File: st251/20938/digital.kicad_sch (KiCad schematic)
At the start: 25 parts, among them Y1 Crystal_Small, Y2 Crystal_Small

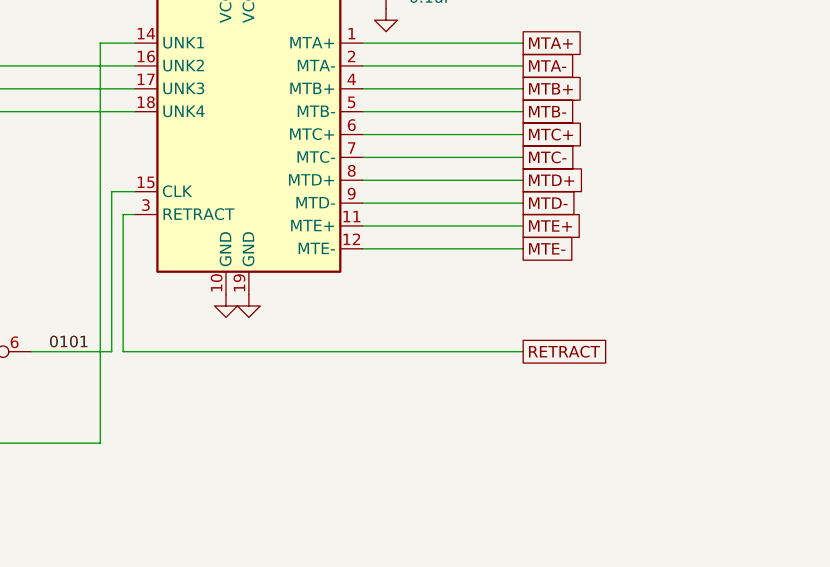
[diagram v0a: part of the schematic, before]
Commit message: Added description for RETURN ASIC
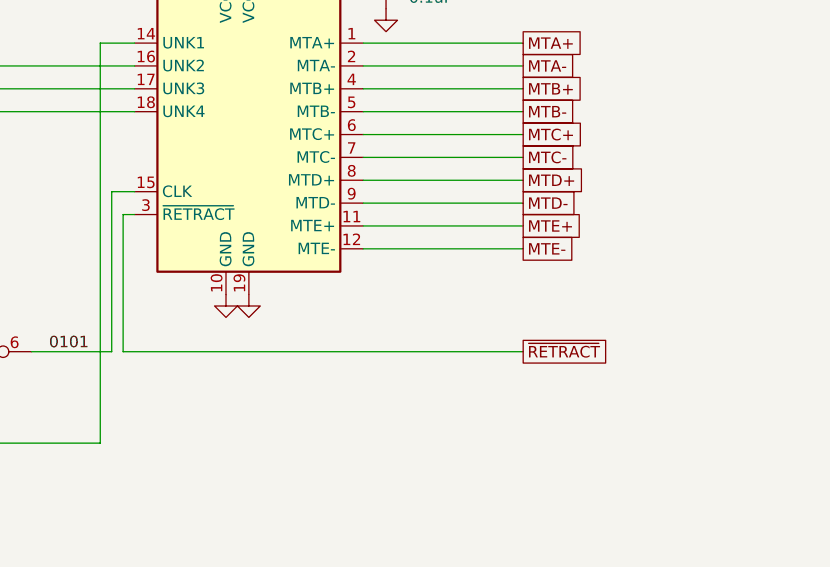
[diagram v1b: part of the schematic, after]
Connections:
- net RETRACT renamed ~{RETRACT}
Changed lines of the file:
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@@
     )
   )
-  (global_label "RETRACT" (shape passive) (at 355.6 139.7 0) (fields_autoplaced)
+  (global_label "~{RETRACT}" (shape passive) (at 355.6 139.7 0) (fields_autoplaced)
     (effects (font (size 1.27 1.27)) (justify left))
     (property "Intersheetrefs" "${INTERSHEET_REFS}" (at 365.4567 139.7 0)

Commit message: Add stepper sequencer documentation
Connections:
- net L_STEP?: now reaches 2B1.39 (UNK14), 3A1.31 (PA2)
- net L_TRK0_OUT: now reaches 2B1.5 (UNK15), 3A1.41 (PB0)
- net ~{HALFSTEP}: now reaches 6C1.16 (Q6), 7C1.16 (~{HALFSTEP})
- net DIRECTION: now reaches 6C1.15 (Q5), 7C1.17 (DIRECTION)
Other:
- note added: "<-"
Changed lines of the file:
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@@
     (stroke (width 0) (type default))
   )
-  (wire (pts (xy 287.02 93.98) (xy 287.02 110.49))
+  (wire (pts (xy 303.53 93.98) (xy 303.53 110.49))
     (stroke (width 0) (type default))
   )
@@
     (stroke (width 0) (type default))
   )
-  (wire (pts (xy 276.86 93.98) (xy 287.02 93.98))
+  (wire (pts (xy 276.86 93.98) (xy 303.53 93.98))
     (stroke (width 0) (type default))
   )
@@
     (stroke (width 0) (type default))
   )
-  (wire (pts (xy 287.02 110.49) (xy 312.42 110.49))
+  (wire (pts (xy 303.53 110.49) (xy 312.42 110.49))
     (stroke (width 0) (type default))
   )
@@
     (stroke (width 0) (type default))
   )
-  (wire (pts (xy 276.86 96.52) (xy 289.56 96.52))
+  (wire (pts (xy 276.86 96.52) (xy 300.99 96.52))
     (stroke (width 0) (type default))
   )
@@
     (stroke (width 0) (type default))
   )
-  (wire (pts (xy 289.56 96.52) (xy 289.56 107.95))
+  (wire (pts (xy 300.99 96.52) (xy 300.99 107.95))
     (stroke (width 0) (type default))
   )
@@
     (stroke (width 0) (type default))
   )
-  (wire (pts (xy 289.56 107.95) (xy 312.42 107.95))
+  (wire (pts (xy 300.99 107.95) (xy 312.42 107.95))
     (stroke (width 0) (type default))
   )
@@
     (effects (font (size 1.27 1.27)) (justify left bottom))
   )
+  (text "<-" (at 71.12 82.55 0)
+    (effects (font (size 1.27 1.27)) (justify left bottom))
+  )
   (text "ST-251 LSI FA CONTROL" (at 302.26 260.35 0)
     (effects (font (size 3.81 3.81)) (justify left bottom))
@@
     (effects (font (size 1.27 1.27)) (justify right bottom))
   )
+  (label "L_TRK0_OUT" (at 74.93 82.55 0) (fields_autoplaced)
+    (effects (font (size 1.27 1.27)) (justify left bottom))
+  )
   (label "L_DIR" (at 73.66 74.93 0) (fields_autoplaced)
     (effects (font (size 1.27 1.27)) (justify left bottom))
@@
     (effects (font (size 1.27 1.27)) (justify left bottom))
   )
+  (label "~{HALFSTEP}" (at 288.29 96.52 0) (fields_autoplaced)
+    (effects (font (size 1.27 1.27)) (justify left bottom))
+  )
   (label "A2" (at 148.59 74.93 180) (fields_autoplaced)
     (effects (font (size 1.27 1.27)) (justify right bottom))
@@
     (effects (font (size 1.27 1.27)) (justify left bottom))
   )
+  (label "INDEX_SYNC" (at 267.97 120.65 0) (fields_autoplaced)
+    (effects (font (size 1.27 1.27)) (justify left bottom))
+  )
+  (label "L_STEP?" (at 73.66 77.47 0) (fields_autoplaced)
+    (effects (font (size 1.27 1.27)) (justify left bottom))
+  )
   (label "D0" (at 160.02 101.6 0) (fields_autoplaced)
     (effects (font (size 1.27 1.27)) (justify left bottom))
@@
     (effects (font (size 1.27 1.27)) (justify right bottom))
   )
+  (label "DIRECTION" (at 292.1 93.98 0) (fields_autoplaced)
+    (effects (font (size 1.27 1.27)) (justify left bottom))
+  )
   (label "PHI2" (at 246.38 149.86 0) (fields_autoplaced)

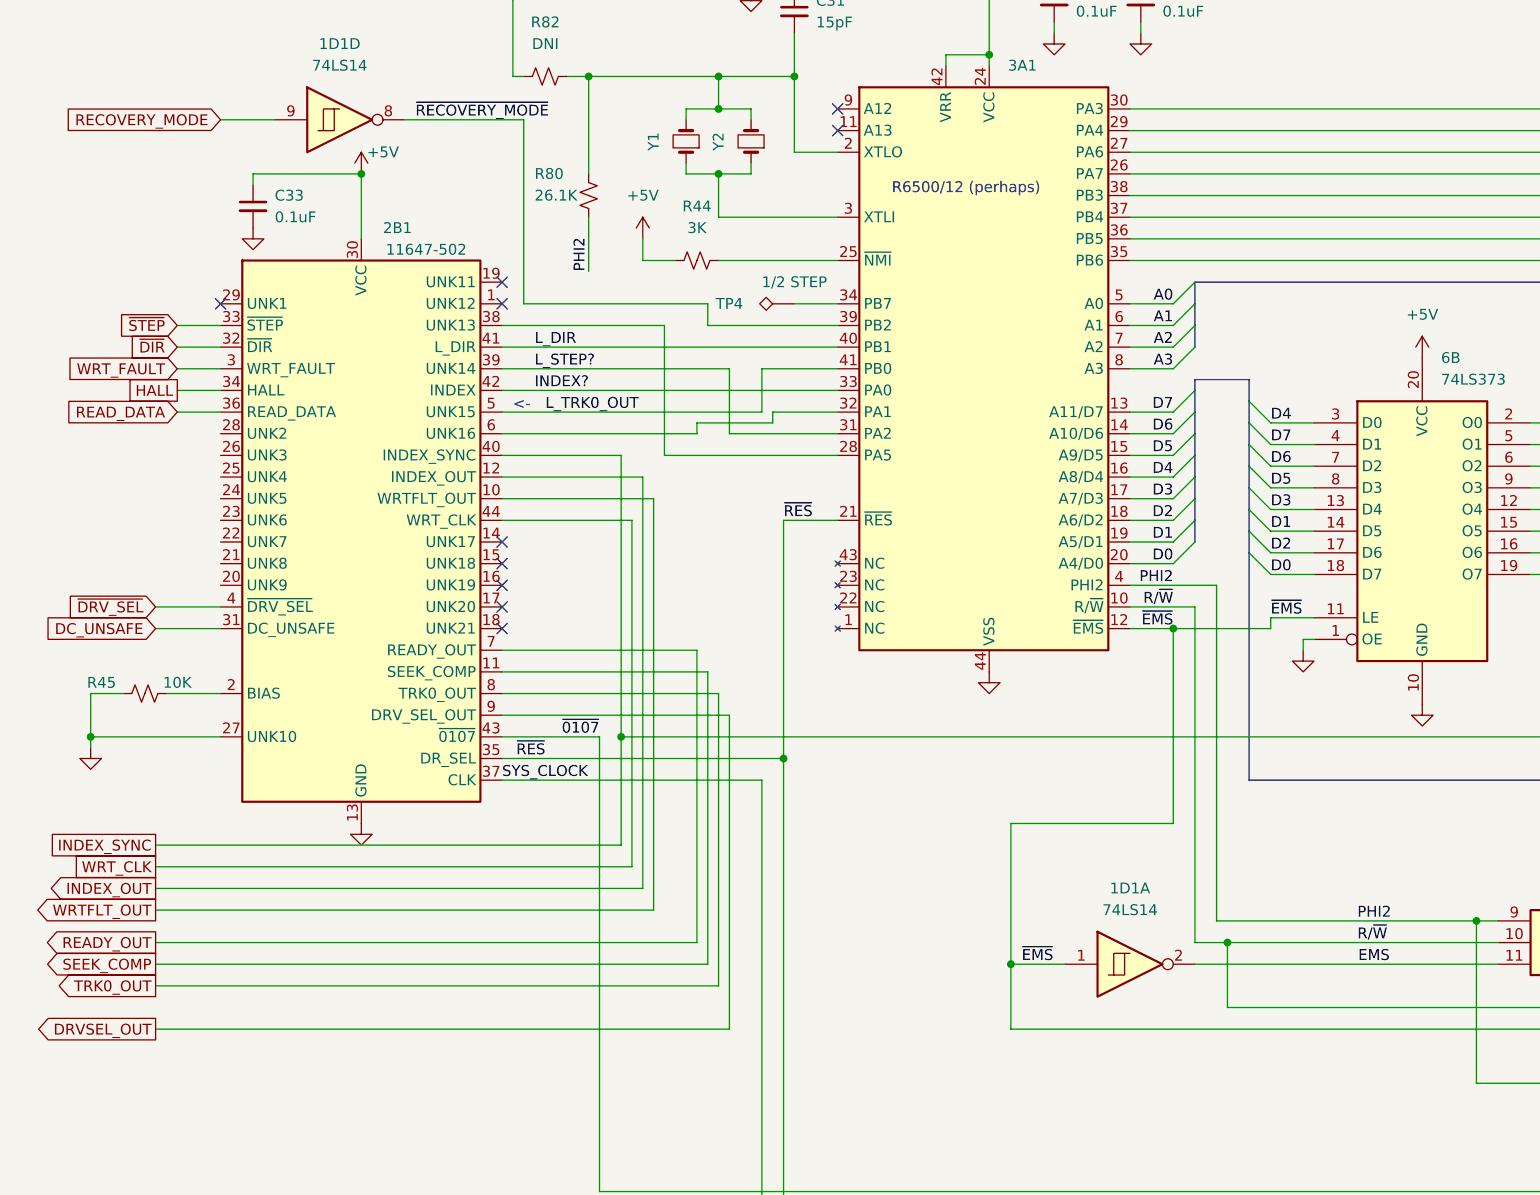
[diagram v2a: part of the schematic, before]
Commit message: Add info on MFM interface IC
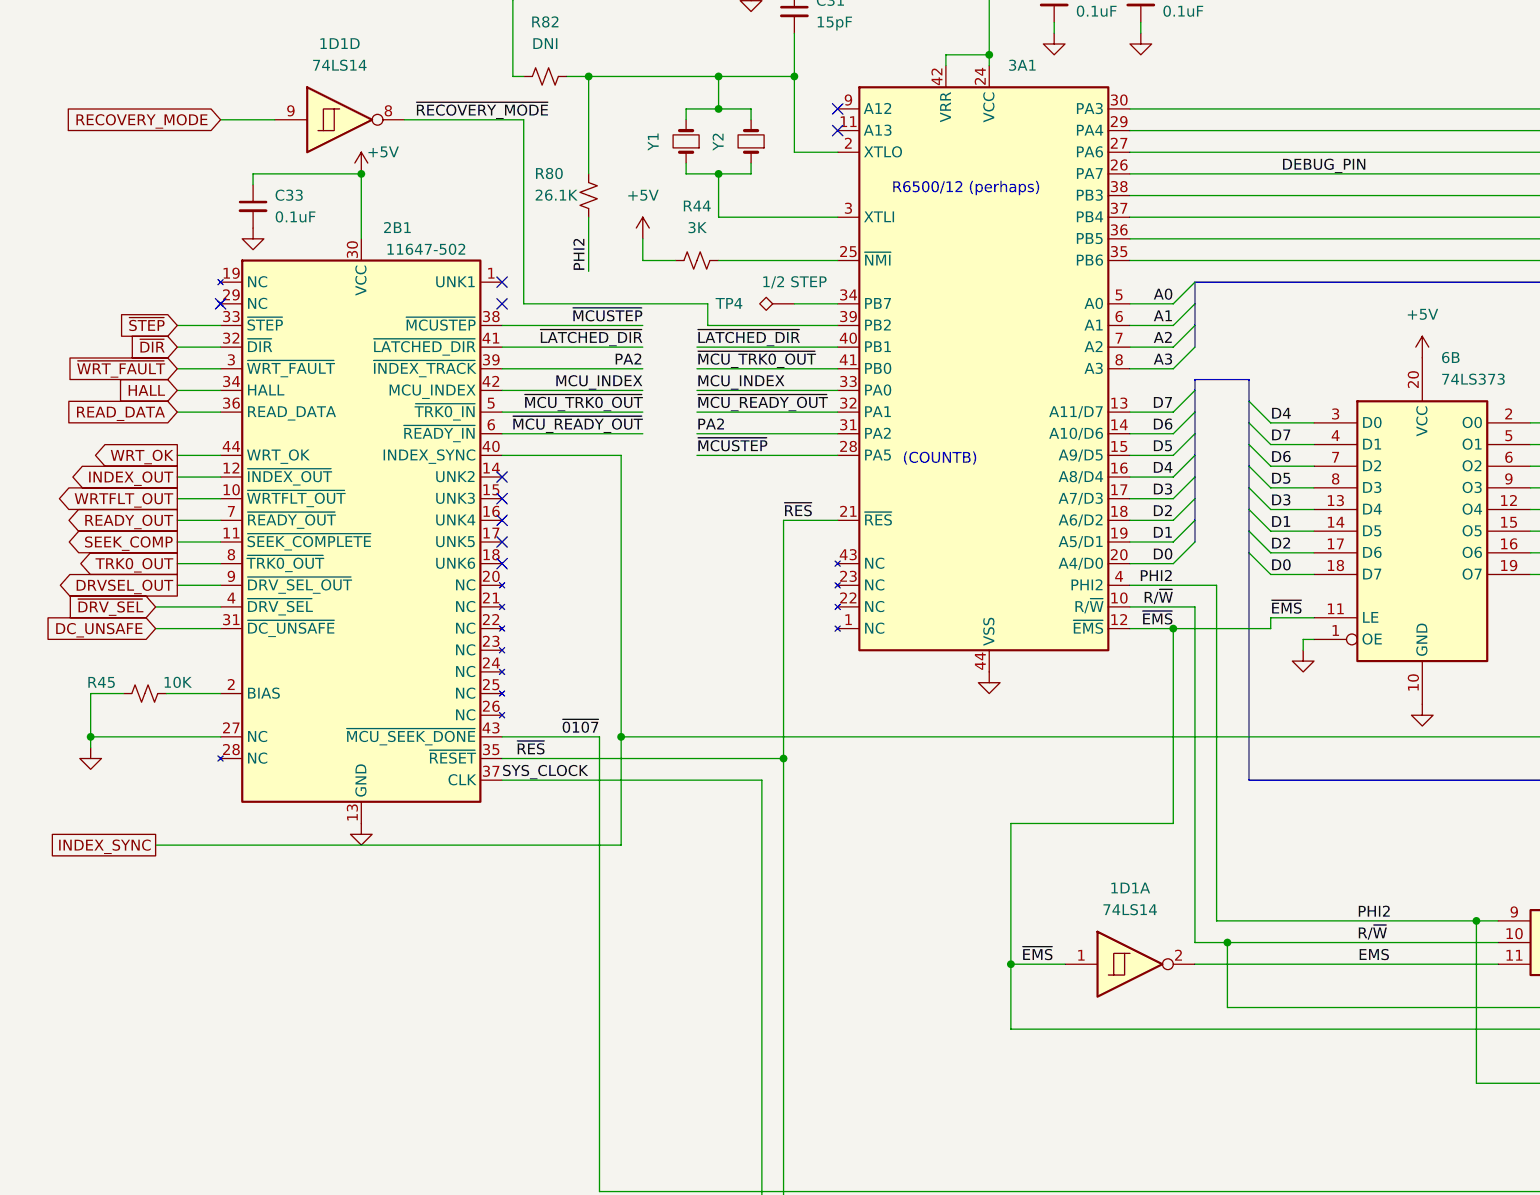
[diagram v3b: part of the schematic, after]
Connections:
- net ~{MCUSTEP}: now reaches 2B1.38 (~{MCUSTEP}), 3A1.28 (PA5)
- net ~{MCU_READY_OUT}: now reaches 2B1.6 (~{READY_IN}), 3A1.32 (PA1)
- net DEBUG_PIN: now reaches 3A1.26 (PA7), R33.1
- net INDEX? renamed MCU_INDEX
- net L_DIR renamed ~{LATCHED_DIR}
- net L_STEP? renamed PA2
- net L_TRK0_OUT renamed ~{MCU_TRK0_OUT}
- net WRT_CLK renamed WRT_OK
- net WRT_FAULT renamed ~{WRT_FAULT}
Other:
- note added: "(COUNTB)"
- note removed: "<-"

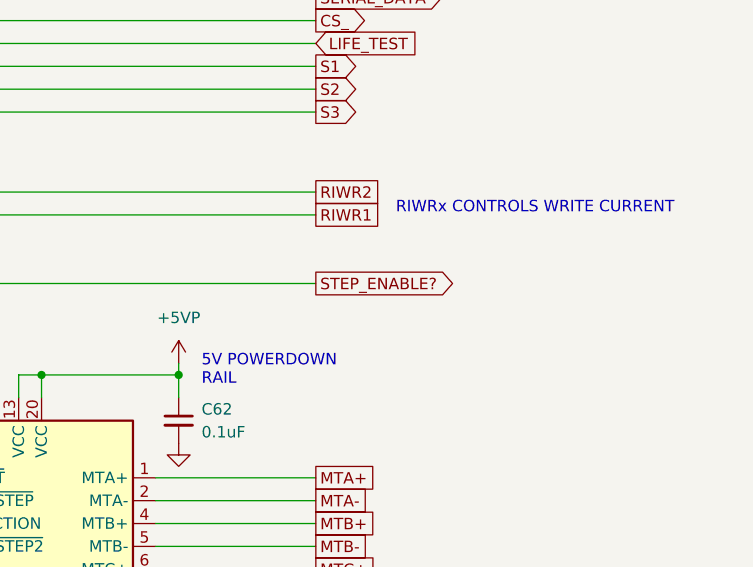
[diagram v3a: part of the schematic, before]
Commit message: Add 11743-501 description (stepper enable driver)
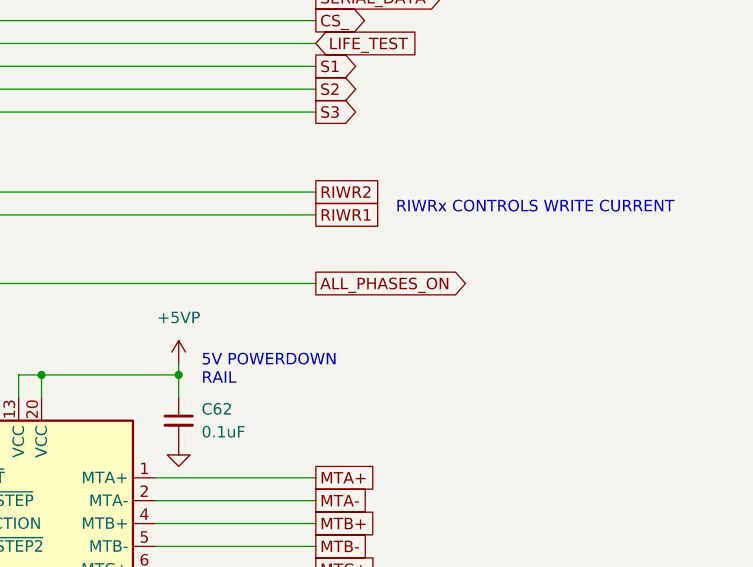
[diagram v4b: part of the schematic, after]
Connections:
- net STEP_ENABLE? renamed ALL_PHASES_ON
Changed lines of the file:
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@@
     )
   )
-  (global_label "STEP_ENABLE?" (shape output) (at 355.6 83.82 0) (fields_autoplaced)
+  (global_label "ALL_PHASES_ON" (shape output) (at 355.6 83.82 0) (fields_autoplaced)
     (effects (font (size 1.27 1.27)) (justify left))
-    (property "Intersheetrefs" "${INTERSHEET_REFS}" (at 372.2527 83.82 0)
+    (property "Intersheetrefs" "${INTERSHEET_REFS}" (at 373.5833 83.82 0)
       (effects (font (size 1.27 1.27)) (justify left) hide)
     )

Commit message: Add ring detector LSI docs
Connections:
- net INDEX_SYNC renamed ~{INDEX_SYNC}
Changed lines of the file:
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@@
     (effects (font (size 1.27 1.27)) (justify left bottom))
   )
-  (label "INDEX_SYNC" (at 267.97 120.65 0) (fields_autoplaced)
+  (label "~{INDEX_SYNC}" (at 267.97 120.65 0) (fields_autoplaced)
     (effects (font (size 1.27 1.27)) (justify left bottom))
   )
@@
     )
   )
-  (global_label "INDEX_SYNC" (shape passive) (at 29.21 133.35 180) (fields_autoplaced)
-    (effects (font (size 1.27 1.27)) (justify right))
-    (property "Intersheetrefs" "${INTERSHEET_REFS}" (at 15.9061 133.35 0)
-      (effects (font (size 1.27 1.27)) (justify right) hide)
-    )
+  (global_label "~{INDEX_SYNC}" (shape output) (at 29.21 133.35 180) (fields_autoplaced)
+    (effects (font (size 1.27 1.27)) (justify right))
+    (property "Intersheetrefs" "${INTERSHEET_REFS}" (at 14.7948 133.35 0)
+      (effects (font (size 1.27 1.27)) (justify right) hide)
+    )

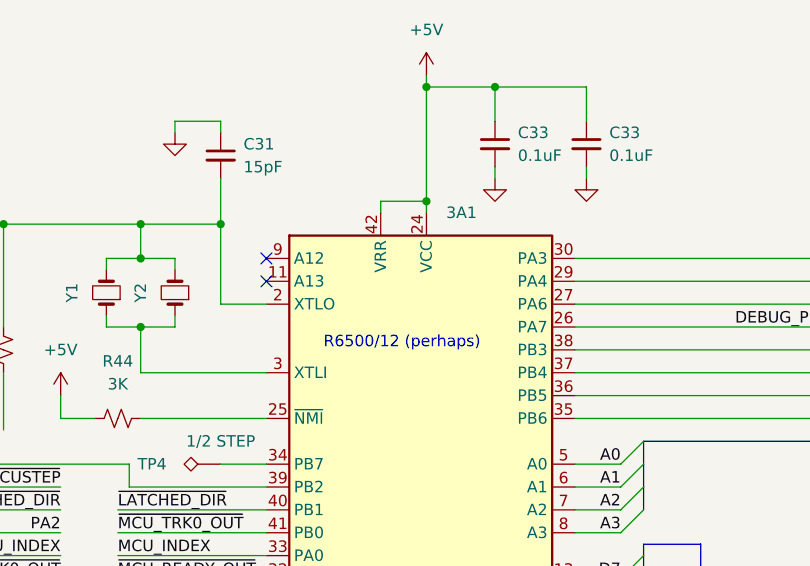
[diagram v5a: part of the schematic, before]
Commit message: fix some spindle motor driver pins
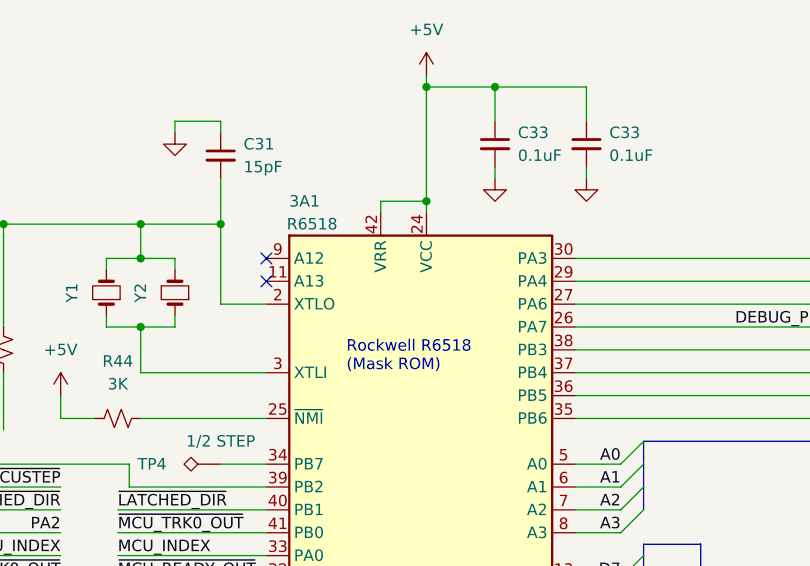
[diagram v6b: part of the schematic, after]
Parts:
- 3A1: value ~ -> R6518
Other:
- note added: "Rockwell R6518 (Mask ROM)"
- note removed: "R6500/12 (perhaps)"
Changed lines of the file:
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@@
     (effects (font (size 1.27 1.27)) (justify left bottom))
   )
-  (text "R6500/12 (perhaps)" (at 115.57 57.15 0)
+  (text "Rockwell R6518\n(Mask ROM)" (at 118.11 59.69 0)
     (effects (font (size 1.27 1.27)) (justify left bottom))
   )
@@
   )
   (symbol (lib_id "st251:6518") (at 111.76 44.45 0) (unit 1)
-    (in_bom yes) (on_board yes) (dnp no) (fields_autoplaced)
-    (property "Reference" "3A1" (at 129.1941 41.91 0)
-      (effects (font (size 1.27 1.27)) (justify left))
-    )
-    (property "Value" "~" (at 111.76 44.45 0)
-      (effects (font (size 1.27 1.27)))
-    )
+    (in_bom yes) (on_board yes) (dnp no)
+    (property "Reference" "3A1" (at 111.76 40.64 0)
+      (effects (font (size 1.27 1.27)) (justify left))
+    )
+    (property "Value" "R6518" (at 114.3 43.18 0)
+      (effects (font (size 1.27 1.27)))
+    )
